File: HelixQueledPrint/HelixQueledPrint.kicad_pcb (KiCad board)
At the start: 4 copper layers, 120 parts, among them J1 USB_C_Receptacle_USB2.0_16P, J101 Conn_Coaxial, J601 Screw_Terminal_01x02, SW1 SW_SPST, SW2 SW_SPST, U101 ESP32-C6FHx, U102 BGS12WN6E6327, U202 TPS92201, U302 TPS92201, U402 TPS92201, U502 TPS92201, U601 MB34F, U602 SY8366H, U603 XBL1117, Y1 40MHz

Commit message: Alles afgerond, geen drc errors meer
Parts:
- removed C602: 68uF 25V, Capacitor_SMD:CP_Elec_6.3x5.4
- added C15: 10uF 25V, Capacitor_SMD:C_0805_2012Metric, F.Cu at (124.7, 79.7)
- added C16: 10uF 25V, Capacitor_SMD:C_0805_2012Metric, F.Cu at (119.3, 69.6)
- added R17: 0R, Resistor_SMD:R_0402_1005Metric, F.Cu at (116.1, 50.3)
- moved R601 4.13 mm to (130.5, 77.3)
- moved R602 1.99 mm to (128.6, 77.3)
- moved C601 1.91 mm to (125.0, 65.7)
- moved C13 1.40 mm to (117.7, 55.1)
- moved C14 1.40 mm to (120.5, 55.1)
- moved L1 1.40 mm to (119.1, 54.6)
- moved C605 1.37 mm to (122.0, 80.2)
- moved R6 0.91 mm to (127.3, 61.3)
- moved J601 0.40 mm to (108.9, 75.9)
- moved U601 0.30 mm to (116.7, 76.6)
- moved R7 0.20 mm to (129.5, 62.2)
- moved L201 0.11 mm to (130.6, 43.5)
- moved L301 0.10 mm to (133.1, 64.3)
- moved C3 0.10 mm to (120.4, 46.9)
- moved L501 0.10 mm to (144.5, 43.9)
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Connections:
- U101 pad 19: unconnected-(U101-GPIO15-Pad19) -> /GPIO15
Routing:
- net /GPIO15: track 0.00 -> 23.8 mm, vias 0 -> 4
- net /PSU/VinDC: track 63.1 -> 57.6 mm
- net GND: track 8.16 -> 5.27 mm, vias 82 -> 208
- net Net-(U602-FB): track 8.85 -> 11.7 mm
- net /PWMG: track 27.5 -> 29.8 mm
- net /GPIO8: track 26.8 -> 24.7 mm
- net Net-(U101-ANT): track 4.03 -> 2.55 mm
- net Net-(U102-RFIN): track 3.06 -> 4.43 mm
- net +5V: track 116.3 -> 117.6 mm, vias 12 -> 11
- net unconnected-(U101-GPIO15-Pad19): track 1.16 -> 0.00 mm, vias 1 -> 0
- net /LedDriverWhite/LED+: track 30.3 -> 31.4 mm
- net /ADC1_CH2: track 9.67 -> 10.7 mm
- net Net-(U102-CTRL): track 3.60 -> 4.49 mm
- net +3V3: track 111.8 -> 112.4 mm
- net /ENW: track 34.2 -> 34.8 mm
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- added copper zone on F.Cu, net /PSU/VinDC
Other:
- board outline added: 47.1 x 43.3 mm

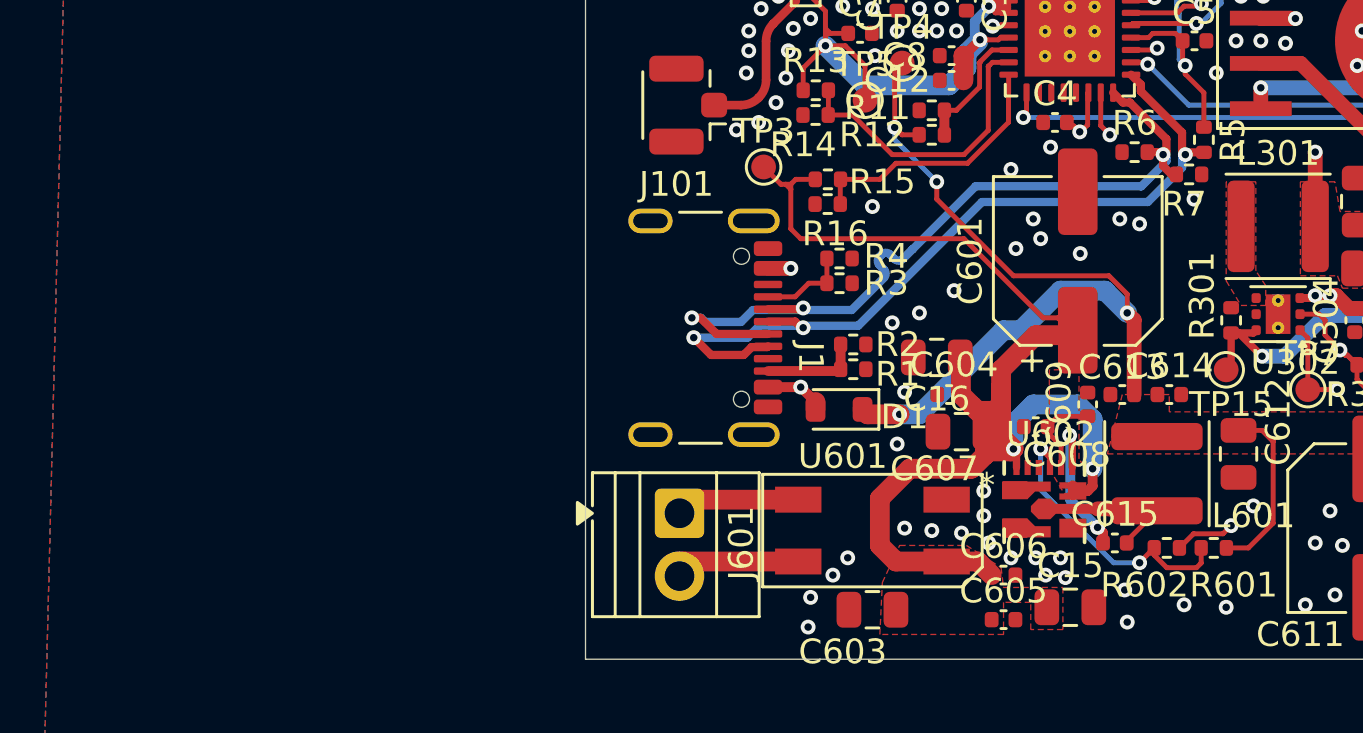
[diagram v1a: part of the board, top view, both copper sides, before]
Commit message: added usb-pd trigger
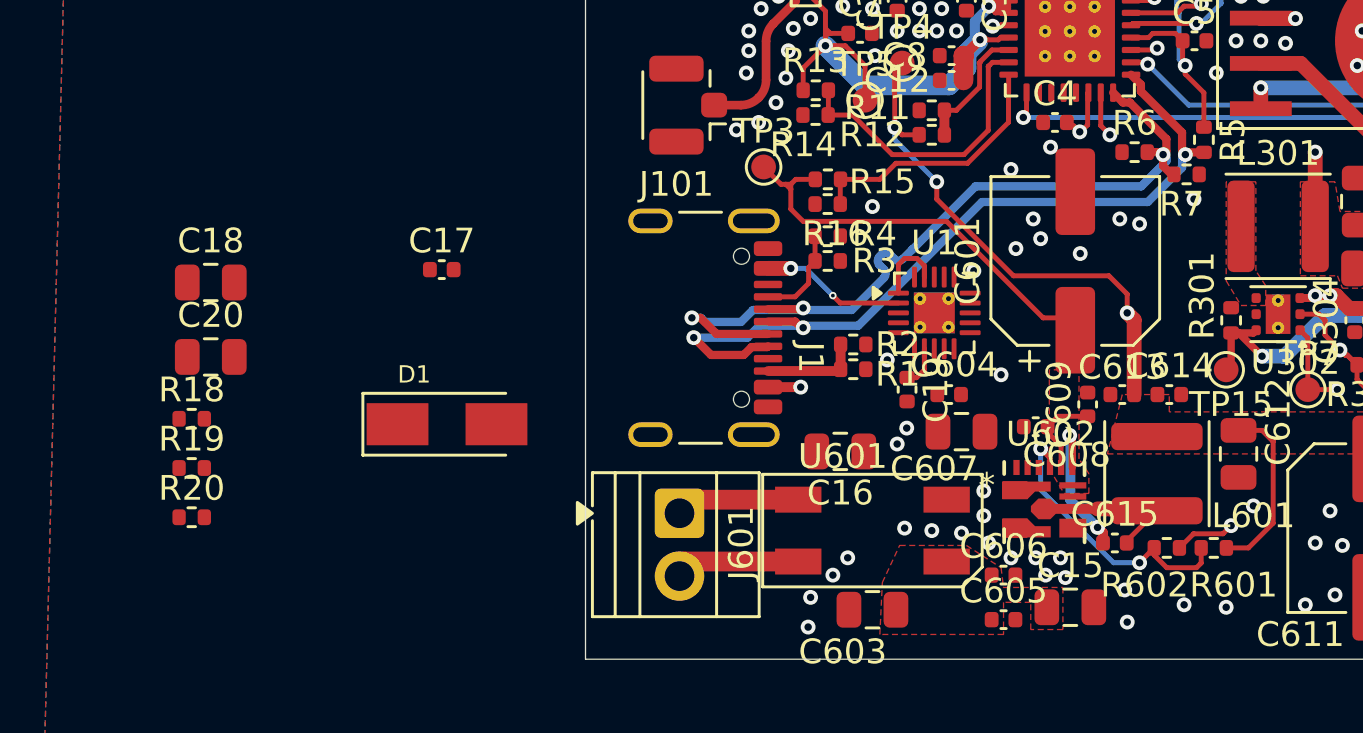
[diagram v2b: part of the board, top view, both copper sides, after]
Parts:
- added C17: 100nF 25V, Capacitor_SMD:C_0402_1005Metric, F.Cu at (99.3, 66.0)
- added C18: 10uF 25V, Capacitor_SMD:C_0805_2012Metric, F.Cu at (90.0, 66.6)
- added C19: 100nF 25V, Capacitor_SMD:C_0402_1005Metric, F.Cu at (118.1, 70.9)
- added C20: 10uF 25V, Capacitor_SMD:C_0805_2012Metric, F.Cu at (90.0, 69.6)
- added R18: 0R, Resistor_SMD:R_0402_1005Metric, F.Cu at (89.2, 72.1)
- added R19: 0R, Resistor_SMD:R_0402_1005Metric, F.Cu at (89.2, 74.1)
- added R20: N.C., Resistor_SMD:R_0402_1005Metric, F.Cu at (89.2, 76.1)
- added U1: CH224D, Package_DFN_QFN:QFN-20-1EP_3x3mm_P0.4mm_EP1.65x1.65mm_ThermalVias, F.Cu at (119.2, 67.8)
- D1: value D_Schottky -> SS34; footprint Diode_SMD:D_SOD-110 -> VE_diodes:SMA
- moved D1 15.9 mm to (99.5, 72.3), turned to 0 degrees
- moved C16 5.45 mm to (115.4, 73.4)
- moved R3 1.02 mm to (114.9, 65.7)
- moved R4 1.02 mm to (114.9, 64.7)
- moved C601 0.10 mm to (124.9, 65.7)
- moved R7 0.10 mm to (129.4, 62.2)
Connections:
- C15 pad 1: /PSU/VinDC -> /Vbus
- C16 pad 1: /PSU/VinDC -> /Vbus
- C601 pad 1: /PSU/VinDC -> /Vbus
- C603 pad 1: /PSU/VinDC -> /Vbus
- C604 pad 1: /PSU/VinDC -> /Vbus
- C605 pad 1: /PSU/VinDC -> /Vbus
- C606 pad 1: /PSU/VinDC -> /Vbus
- C607 pad 1: /PSU/VinDC -> /Vbus
- D1 pad 1: +5V -> /Vbus
- R15 pad 2: /PSU/VinDC -> /Vbus
- TP3 pad 1: /PSU/VinDC -> /Vbus
- U601 pad 1: /PSU/VinDC -> /Vbus
- U602 pad 12: /PSU/VinDC -> /Vbus
- U602 pad 5: /PSU/VinDC -> /Vbus
- U602 pad 6: /PSU/VinDC -> /Vbus
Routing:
- net /PSU/VinDC: track 57.6 -> 0.00 mm, vias 2 -> 0
- net /Vbus: track 0.00 -> 17.2 mm
- net +5V: track 117.6 -> 104.3 mm, vias 11 -> 10
- net Net-(D1-A): track 8.56 -> 12.3 mm, vias 2 -> 3
- net Net-(U1-DRV): track 0.00 -> 2.88 mm
- net Net-(U1-VDD): track 0.00 -> 1.68 mm
- added copper zone on F.Cu, net /Vbus
- removed copper zone on F.Cu, net /PSU/VinDC

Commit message: finished (i think)
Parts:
- removed R101, R102, R17: 0R, Resistor_SMD:R_0402_1005Metric
- removed U102: BGS12WN6E6327, Package_LGA:Infineon_PG-TSNP-6-10_0.7x1.1mm_0.7x1.1mm_P0.4mm
- added C101: C, Capacitor_SMD:C_0402_1005Metric, F.Cu at (114.5, 54.7)
- added C102: C, Capacitor_SMD:C_0402_1005Metric, F.Cu at (114.9, 54.4)
- added C103: C, Capacitor_SMD:C_0402_1005Metric, F.Cu at (114.9, 54.9)
- D1: moved to B.Cu
- moved R20 33.1 mm to (120.4, 65.1)
- moved C18 29.1 mm to (118.9, 63.6)
- moved R19 26.9 mm to (115.4, 68.1)
- moved R18 26.7 mm to (115.4, 67.1)
- moved C20 25.7 mm to (115.6, 71.6), turned to 180 degrees
- moved C17 17.6 mm to (116.9, 65.6), turned to 90 degrees
- moved D1 15.5 mm to (114.2, 77.1), turned to 90 degrees
- moved C603 2.60 mm to (119.3, 79.9)
- moved C604 1.60 mm to (121.4, 71.1)
- moved C614 0.73 mm to (129.4, 71.3)
- moved C613 0.73 mm to (127.5, 71.3)
- moved C609 0.70 mm to (124.7, 71.5)
- moved C16 0.20 mm to (115.4, 73.6)
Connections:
- U1 pad 21: (no net) -> GND
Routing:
- net /Vbus: track 17.2 -> 60.6 mm, vias 0 -> 5
- net /GPIO15: track 23.8 -> 0.00 mm, vias 4 -> 0
- net Net-(J1-CC1): track 3.88 -> 23.4 mm, vias 0 -> 2
- net +3V3: track 112.4 -> 103.0 mm, vias 10 -> 9
- net Net-(J1-CC2): track 3.86 -> 12.8 mm, vias 0 -> 2
- net Net-(D1-A): track 12.3 -> 21.0 mm
- net Net-(U1-DN): track 0.00 -> 6.27 mm, vias 0 -> 2
- net Net-(U1-DP): track 0.00 -> 5.62 mm, vias 0 -> 2
- net Net-(U102-CTRL): track 4.49 -> 0.00 mm
- net Net-(U1-VDD): track 1.68 -> 3.72 mm
- net Net-(U1-DRV): track 2.88 -> 4.84 mm
- net /USB_D-: track 33.5 -> 34.8 mm
- net /USB_D+: track 33.1 -> 34.4 mm
- net Net-(C102-Pad2): track 4.43 -> 3.29 mm
- net GND: track 5.27 -> 4.20 mm, vias 208 -> 239
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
